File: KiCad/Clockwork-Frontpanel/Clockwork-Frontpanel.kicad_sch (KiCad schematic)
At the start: 15 parts

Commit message: New Gerbers, added the xtal to the BOM, new MH for OLED
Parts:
- D1, D2: footprint easyEDA:LED-SMD_L3.2-W1.6-FD_EH-GREEN-1 -> easyEDA:LED-SMD_L3.2-W1.6-RD-EH-3_kicad
- D3: footprint (none) -> easyEDA:LED-SMD_L3.2-W1.6-RD-EH-3_kicad
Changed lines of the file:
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@@
 			)
 		)
-		(property "Footprint" "easyEDA:LED-SMD_L3.2-W1.6-FD_EH-GREEN-1"
+		(property "Footprint" "easyEDA:LED-SMD_L3.2-W1.6-RD-EH-3_kicad"
 			(at 120.65 59.69 90)
 			(effects
@@
 			)
 		)
-		(property "Footprint" ""
+		(property "Footprint" "easyEDA:LED-SMD_L3.2-W1.6-RD-EH-3_kicad"
 			(at 120.65 62.23 90)
 			(effects
@@
 			)
 		)
-		(property "Footprint" "easyEDA:LED-SMD_L3.2-W1.6-FD_EH-GREEN-1"
+		(property "Footprint" "easyEDA:LED-SMD_L3.2-W1.6-RD-EH-3_kicad"
 			(at 120.65 57.15 90)
 			(effects

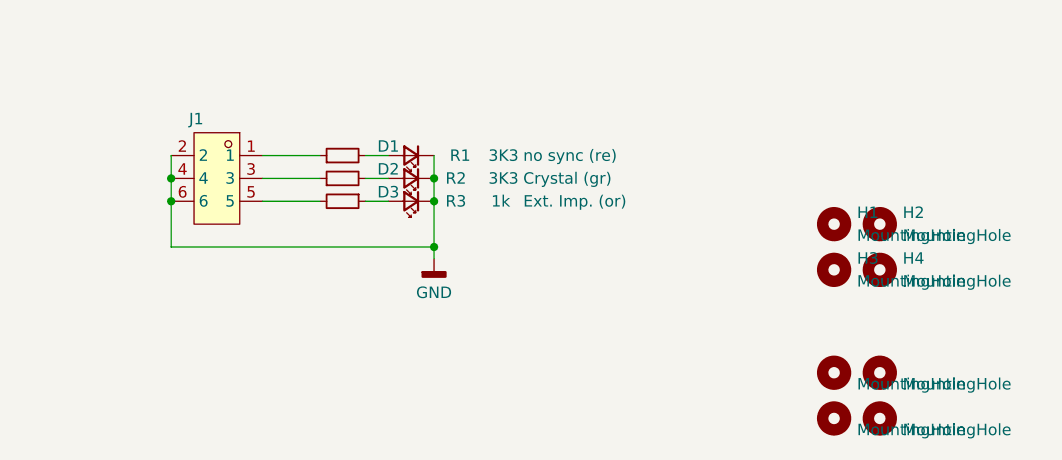
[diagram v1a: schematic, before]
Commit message: Fixing the Pin Numbering Mess for the Frontpanel LEDs, also, polarity of ESS in LED
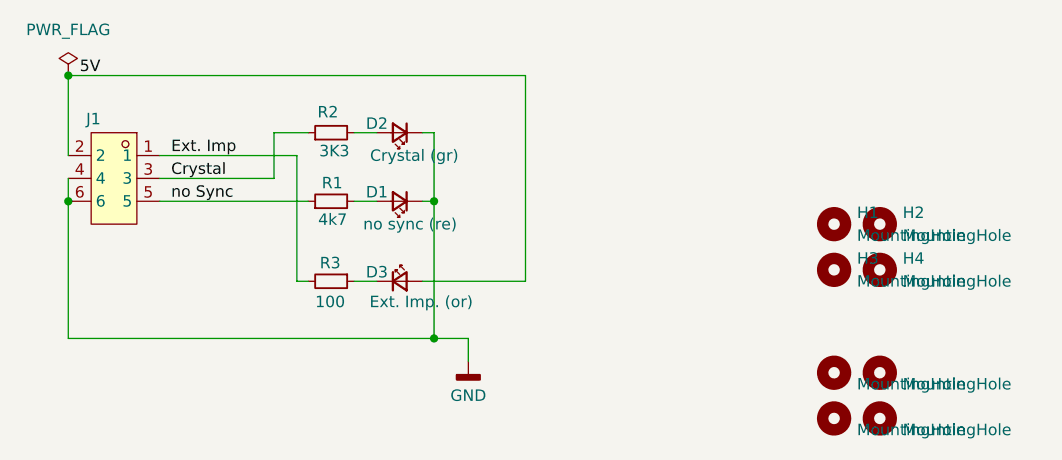
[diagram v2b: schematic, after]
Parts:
- J1: footprint easyEDA:HDR-SMD_6P-P2.00-V-M-R2-C3-LS6.5 -> easyEDA:HDR-SMD_6P-P2.00-V-M-R2-C3-LS6.5_flipped
- R1: value 3K3 -> 4k7; LCSC C22978 -> (none)
- R3: value 1k -> 100; LCSC C21190 -> (none)
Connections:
- net GND: no longer D3.1 (K), J1.2
- net Ext. Imp: now reaches J1.1
- net Ext. Imp: now also R3.2; no longer R1.1
- net Crystal: now reaches J1.3, R2.1
- net no Sync: now reaches J1.5
- net no Sync: now also R1.1; no longer R3.2
- net at R3.1: now also D3.1 (K); no longer D3.2 (A)
- new net 5V: D3.2 (A), J1.2
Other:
- moved on the sheet: D1, D2, D3, J1, R1, R2, R3

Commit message: Updated Resistor Values, Button Holes 0.3mm bigger, Display Rect 1mm lower, new LED Labels, Moved GND Via
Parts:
- H5, H6, H7, H8: footprint MountingHole:MountingHole_3.2mm_M3_DIN965 -> Peacemans Teile:MountingHole_3.5mm_M3
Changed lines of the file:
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@@
 			)
 		)
-		(property "Footprint" "MountingHole:MountingHole_3.2mm_M3_DIN965"
+		(property "Footprint" "Peacemans Teile:MountingHole_3.5mm_M3"
 			(at 167.64 81.28 0)
 			(effects
@@
 			)
 		)
-		(property "Footprint" "MountingHole:MountingHole_3.2mm_M3_DIN965"
+		(property "Footprint" "Peacemans Teile:MountingHole_3.5mm_M3"
 			(at 172.72 81.28 0)
 			(effects
@@
 			)
 		)
-		(property "Footprint" "MountingHole:MountingHole_3.2mm_M3_DIN965"
+		(property "Footprint" "Peacemans Teile:MountingHole_3.5mm_M3"
 			(at 172.72 86.36 0)
 			(effects
@@
 			)
 		)
-		(property "Footprint" "MountingHole:MountingHole_3.2mm_M3_DIN965"
+		(property "Footprint" "Peacemans Teile:MountingHole_3.5mm_M3"
 			(at 167.64 86.36 0)
 			(effects
